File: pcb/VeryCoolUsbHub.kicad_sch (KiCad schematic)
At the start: 51 parts, among them U1 HD3SS3220RNHR, U2 HD3SS3220RNHR, X1 X322525MSB4SI, X2 X322525MSB4SI

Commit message: please tell me this is the last time i need to reroute
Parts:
- removed C10: CC0603KRX7R9BB104, EasyEDA:C0603, symbol EasyEDA:CC0603KRX7R9BB104
- removed USB_OUT1, USB_OUT2: HC-USB3.0-L168-WP, EasyEDA:USB-TH_USB3.0-A, symbol EasyEDA:HC-USB3.0-L168-WP
- added C33, C34, C35, C36, C37: CC0603KRX7R9BB104, EasyEDA:C0603, symbol EasyEDA:CC0603KRX7R9BB104
- added R4: R, Resistor_SMD:R_0402_1005Metric, symbol Device:R
- added USB_OUT_1, USB_OUT_2: HC-ST-003-01-J, EasyEDA:USB-3.0-A-TH_HC-ST-003-01-Z, symbol EasyEDA:HC-ST-003-01-J
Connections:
- net DN1: now also USB_OUT_1.2 (D-)
- net DN2: now also USB_OUT_2.2 (D-)
- net DP1: now also USB_OUT_1.3 (D+)
- net DP2: now also USB_OUT_2.3 (D+)
- net GND: now also USBC_OUT_1.0 (EH), C34.2, C35.2, R4.2, USB_OUT_1.10 (SHELL), USB_OUT_1.11 (SHELL), USB_OUT_1.4 (GND), USB_OUT_1.7 (GND_DRAIN), USB_OUT_2.10 (SHELL), USB_OUT_2.4 (GND), USB_OUT_2.7 (GND_DRAIN); no longer C11.2
- net VBUS: now also C34.1, USB_OUT_1.1 (Vbus); no longer C11.1
- net at ETHERNET_CONTROLLER1.38 (RSET): now also R4.1
- net RXn0 renamed RXN0
- net RXn1 renamed RXN1
- net RXN1: now also USB_OUT_1.5 (StdA_SSRX-)
- net RXn2 renamed RXN2
- net RXN2: now also USB_OUT_2.5 (StdA_SSRX-)
- net RXn3 renamed RXN3
- net RXn4 renamed RXN4
- net RXp0 renamed RXP0
- net RXp1 renamed RXP1
- net RXP1: now also USB_OUT_1.6 (StdA_SSRX+)
- net RXp2 renamed RXP2
- net RXP2: now also USB_OUT_2.6 (StdA_SSRX+)
- net RXp3 renamed RXP3
- net RXp4 renamed RXP4
- net Txn0 renamed TXN0
- net Txn1 renamed TXN1
- net TXN1: now also C11.2
- net Txn2 renamed TXN2
- net TXN2: now also C36.2
- net Txn3 renamed TXN3
- net Txn4 renamed TXN4
- net Txp0 renamed TXP0
- net Txp1 renamed TXP1
- net TXP1: now also C33.2
- net Txp2 renamed TXP2
- net TXP2: now also C37.2
- net Txp3 renamed TXP3
- net Txp4 renamed TXP4
- new net: C33.1, USB_OUT_1.9 (StdA_SSTX+)
- new net: C37.1, USB_OUT_2.9 (StdA_SSTX+)
- new net: C11.1, USB_OUT_1.8 (StdA_SSTX-)
- new net: C36.1, USB_OUT_2.8 (StdA_SSTX-)
- new net: C35.1, USB_OUT_2.1 (Vbus)

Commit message: LETSGO THIS GONNA BE THE LAST TIME I ROUTE
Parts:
- added C10, C26: CC0603KRX7R9BB104, EasyEDA:C0603, symbol EasyEDA:CC0603KRX7R9BB104
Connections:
- net RXN1: now also USB_OUT_1.6 (StdA_SSRX+); no longer USB_OUT_1.5 (StdA_SSRX-)
- net RXN2: now also USB_OUT_2.6 (StdA_SSRX+); no longer USB_OUT_2.5 (StdA_SSRX-)
- net RXN4: now also ETHERNET_CONTROLLER1.16 (U3SSRXP); no longer ETHERNET_CONTROLLER1.15 (U3SSRXN)
- net RXP1: now also USB_OUT_1.5 (StdA_SSRX-); no longer USB_OUT_1.6 (StdA_SSRX+)
- net RXP2: now also USB_OUT_2.5 (StdA_SSRX-); no longer USB_OUT_2.6 (StdA_SSRX+)
- net RXP4: now also ETHERNET_CONTROLLER1.15 (U3SSRXN); no longer ETHERNET_CONTROLLER1.16 (U3SSRXP)
- net TXN1: now also C33.2; no longer C11.2
- net TXN2: now also C37.2; no longer C36.2
- net TXN4: now also ETHERNET_CONTROLLER1.13 (U3SSTXP); no longer ETHERNET_CONTROLLER1.12 (U3SSTXN)
- net TXP1: now also C11.2; no longer C33.2
- net TXP2: now also C36.2; no longer C37.2
- net TXP4: now also ETHERNET_CONTROLLER1.12 (U3SSTXN); no longer ETHERNET_CONTROLLER1.13 (U3SSTXP)
- net USBC_IN_TXN1: now also C9.2; no longer C8.1
- net USBC_IN_TXN2: now also C20.1; no longer C21.1
- net USBC_IN_TXP1: now also C8.1; no longer C9.2
- net USBC_IN_TXP2: now also C21.1; no longer C20.1
- net USBC_OUT_TXN1: now also C10.2; no longer U1.16 (TX1n)
- net USBC_OUT_TXN2: now also C23.1; no longer C24.1
- net USBC_OUT_TXP1: now also C26.1; no longer U1.17 (TX1p)
- net USBC_OUT_TXP2: now also C24.1; no longer C23.1
- net VBUS: now also C35.1, USB_OUT_2.1 (Vbus)
- new net: C10.1, U1.17 (TX1p)
- new net: C26.2, U1.16 (TX1n)
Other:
- moved on the sheet: C9

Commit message: maybedone?
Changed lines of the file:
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@@
 		)
 		(property "Description" "10kΩ ±1%/62.5mW/0402"
-			(at 99.568 255.016 0)
+			(at 98.806 255.016 0)
 			(effects
 				(font
@@
 			)
 		)
-		(property "Datasheet" "https://www.lcsc.com/datasheet/C871499.pdf"
+		(property "Datasheet" "https://www.lcsc.com/datasheet/C871726.pdf"
 			(at 193.04 93.98 0)
 			(effects

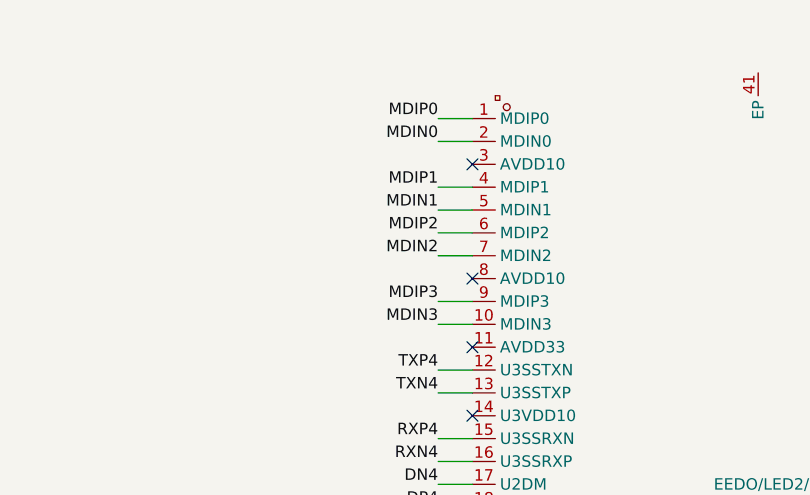
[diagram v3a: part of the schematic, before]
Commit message: reroute a litlle bit of ethernet port
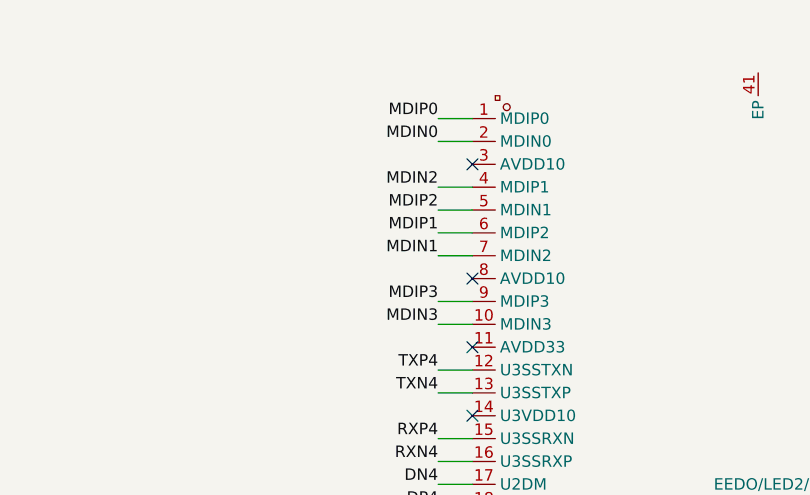
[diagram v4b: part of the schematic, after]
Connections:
- net MDIN1: now also ETHERNET_CONTROLLER1.7 (MDIN2); no longer ETHERNET_CONTROLLER1.5 (MDIN1)
- net MDIN2: now also ETHERNET_CONTROLLER1.4 (MDIP1); no longer ETHERNET_CONTROLLER1.7 (MDIN2)
- net MDIP1: now also ETHERNET_CONTROLLER1.6 (MDIP2); no longer ETHERNET_CONTROLLER1.4 (MDIP1)
- net MDIP2: now also ETHERNET_CONTROLLER1.5 (MDIN1); no longer ETHERNET_CONTROLLER1.6 (MDIP2)
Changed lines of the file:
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@@
-		)
-	)
-	(label "MDIN2"
-		(at 438.15 52.07 180)
-		(effects
-			(font
-				(size 1.27 1.27)
-			)
-			(justify right bottom)
 		)
 	)
@@
 		)
 	)
+	(label "MDIN1"
+		(at 438.15 52.07 180)
+		(effects
+			(font
+				(size 1.27 1.27)
+			)
+			(justify right bottom)
+		)
+	)
 	(label "TXP2"
 		(at 147.32 217.17 0)
@@
 		)
 	)
-	(label "MDIP1"
-		(at 438.15 44.45 180)
-		(effects
-			(font
-				(size 1.27 1.27)
-			)
-			(justify right bottom)
-		)
-	)
 	(label "RXN2"
 		(at 147.32 212.09 0)
@@
 		)
 	)
-	(label "MDIP2"
-		(at 438.15 49.53 180)
-		(effects
-			(font
-				(size 1.27 1.27)
-			)
-			(justify right bottom)
-		)
-	)
 	(label "RXP3"
 		(at 104.14 209.55 180)
@@
 		)
 	)
+	(label "MDIP1"
+		(at 438.15 49.53 180)
+		(effects
+			(font
+				(size 1.27 1.27)
+			)
+			(justify right bottom)
+		)
+	)
 	(label "USBC_OUT_RXP1"
 		(at 83.82 92.71 180)
@@
 		)
 	)
+	(label "MDIP2"
+		(at 438.15 46.99 180)
+		(effects
+			(font
+				(size 1.27 1.27)
+			)
+			(justify right bottom)
+		)
+	)
 	(label "RXN0"
 		(at 146.05 257.81 0)
@@
 		)
 	)
+	(label "MDIN2"
+		(at 438.15 44.45 180)
+		(effects
+			(font
+				(size 1.27 1.27)
+			)
+			(justify right bottom)
+		)
+	)
 	(label "USBC_IN_TXN2"
 		(at 295.91 347.98 180)
@@
 		(effects
 			(font
-				(size 1.27 1.27)
-			)
-			(justify right bottom)
-		)
-	)
-	(label "MDIN1"
-		(at 438.15 46.99 180)
-		(effects
-			(font

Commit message: change schen
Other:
- note added: "ETHERNET"
- note added: "USB A OUT"
- note added: "USB C IN"
- note added: "USB C OUT"
- note added: "USB CONTROLLER"
- moved on the sheet: C17, C18, C25, C5, R2, R3, USB_CONTROLLER1, X2

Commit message: forgor to update
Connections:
- net USB_TXN1: now reaches C33.1, USB_OUT_1.9 (StdA_SSTX+)
- net TXN2+: now reaches C37.1, USB_OUT_2.9 (StdA_SSTX+)
- net IN_C_TXN2: now reaches C20.2, U2.21 (TX2p)
- net USB_TXP1: now reaches C11.1, USB_OUT_1.8 (StdA_SSTX-)
- net IN_C_TXP2: now reaches C21.2, U2.20 (TX2n)
- net C_TXN1: now reaches C10.1, U1.17 (TX1p)
- net C_TXN2: now reaches C23.2, U1.21 (TX2p)
- net TXN2-: now reaches C36.1, USB_OUT_2.8 (StdA_SSTX-)
- net IN_C_TXP1: now reaches C8.2, U2.16 (TX1n)
- net C_TXP2: now reaches C24.2, U1.20 (TX2n)
- net C_TXP1: now reaches C26.2, U1.16 (TX1n)
- net IN_C_TXN1: now reaches C9.1, U2.17 (TX1p)
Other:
- moved on the sheet: C10, C20, C23, C24

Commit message: fixed some signal intergrity problem
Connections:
- net GND: now also U1.31 (EP), U2.31 (EP)
- no-connect marks 60 -> 58
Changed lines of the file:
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@@
 	)
 	(no_connect
-		(at 270.51 55.88)
-	)
-	(no_connect
 		(at 288.29 219.71)
 	)
 	(no_connect
-		(at 464.82 284.48)
-	)
-	(no_connect
 		(at 474.98 284.48)
 	)
@@
 	)
 	(symbol
+		(lib_id "power:GND")
+		(at 270.51 55.88 180)
+		(unit 1)
+		(exclude_from_sim no)
+		(in_bom yes)
+		(on_board yes)
+		(dnp no)
+		(fields_autoplaced yes)
+		(property "Reference" "#PWR029"
+			(at 270.51 49.53 0)
+			(effects
+				(font
+					(size 1.27 1.27)
+				)
+				(hide yes)
+			)
+		)
+		(property "Value" "GND"
+			(at 270.51 50.8 0)
+			(effects
+				(font
+					(size 1.27 1.27)
+				)
+			)
+		)
+		(property "Footprint" ""
+			(at 270.51 55.88 0)
+			(effects
+				(font
+					(size 1.27 1.27)
+				)
+				(hide yes)
+			)
+		)
+		(property "Datasheet" ""
+			(at 270.51 55.88 0)
+			(effects
+				(font
+					(size 1.27 1.27)
+				)
+				(hide yes)
+			)
+		)
+		(property "Description" "Power symbol creates a global label with name \"GND\" , ground"
+			(at 270.51 55.88 0)
+			(effects
+				(font
+					(size 1.27 1.27)
+				)
+				(hide yes)
+			)
+		)
+		(pin "1"
+		)
+		(instances
+			(project "VeryCoolUsbHub"
+				(path "/a66e963d-9223-4dd6-b11b-c5e7c640f212"
+					(reference "#PWR029")
+					(unit 1)
+				)
+			)
+		)
+	)
+	(symbol
 		(lib_id "EasyEDA:RC0603FR-07200KL")
 		(at 454.66 350.52 0)
@@
 					(unit 1)
 				)
+			)
+		)
+	)
+	(symbol
+		(lib_id "power:GND")
+		(at 464.82 284.48 180)
+		(unit 1)
+		(exclude_from_sim no)
+		(in_bom yes)
+		(on_board yes)
+		(dnp no)
+		(fields_autoplaced yes)
+		(property "Reference" "#PWR034"
+			(at 464.82 278.13 0)
+			(effects
+				(font
+					(size 1.27 1.27)
+				)
+				(hide yes)
+			)
+		)
+		(property "Value" "GND"
+			(at 464.82 279.4 0)
+			(effects
+				(font
+					(size 1.27 1.27)
+				)
+			)
+		)
+		(property "Footprint" ""
+			(at 464.82 284.48 0)
+			(effects
+				(font
+					(size 1.27 1.27)
+				)
+				(hide yes)
+			)
+		)
+		(property "Datasheet" ""
+			(at 464.82 284.48 0)
+			(effects
+				(font
+					(size 1.27 1.27)
+				)
+				(hide yes)
+			)
+		)
+		(property "Description" "Power symbol creates a global label with name \"GND\" , ground"
+			(at 464.82 284.48 0)
+			(effects
+				(font
+					(size 1.27 1.27)
+				)
+				(hide yes)
+			)
+		)
+		(pin "1"
+		)
+		(instances
+			(project "VeryCoolUsbHub"
+				(path "/a66e963d-9223-4dd6-b11b-c5e7c640f212"
+					(reference "#PWR034")
+					(unit 1)
+				)

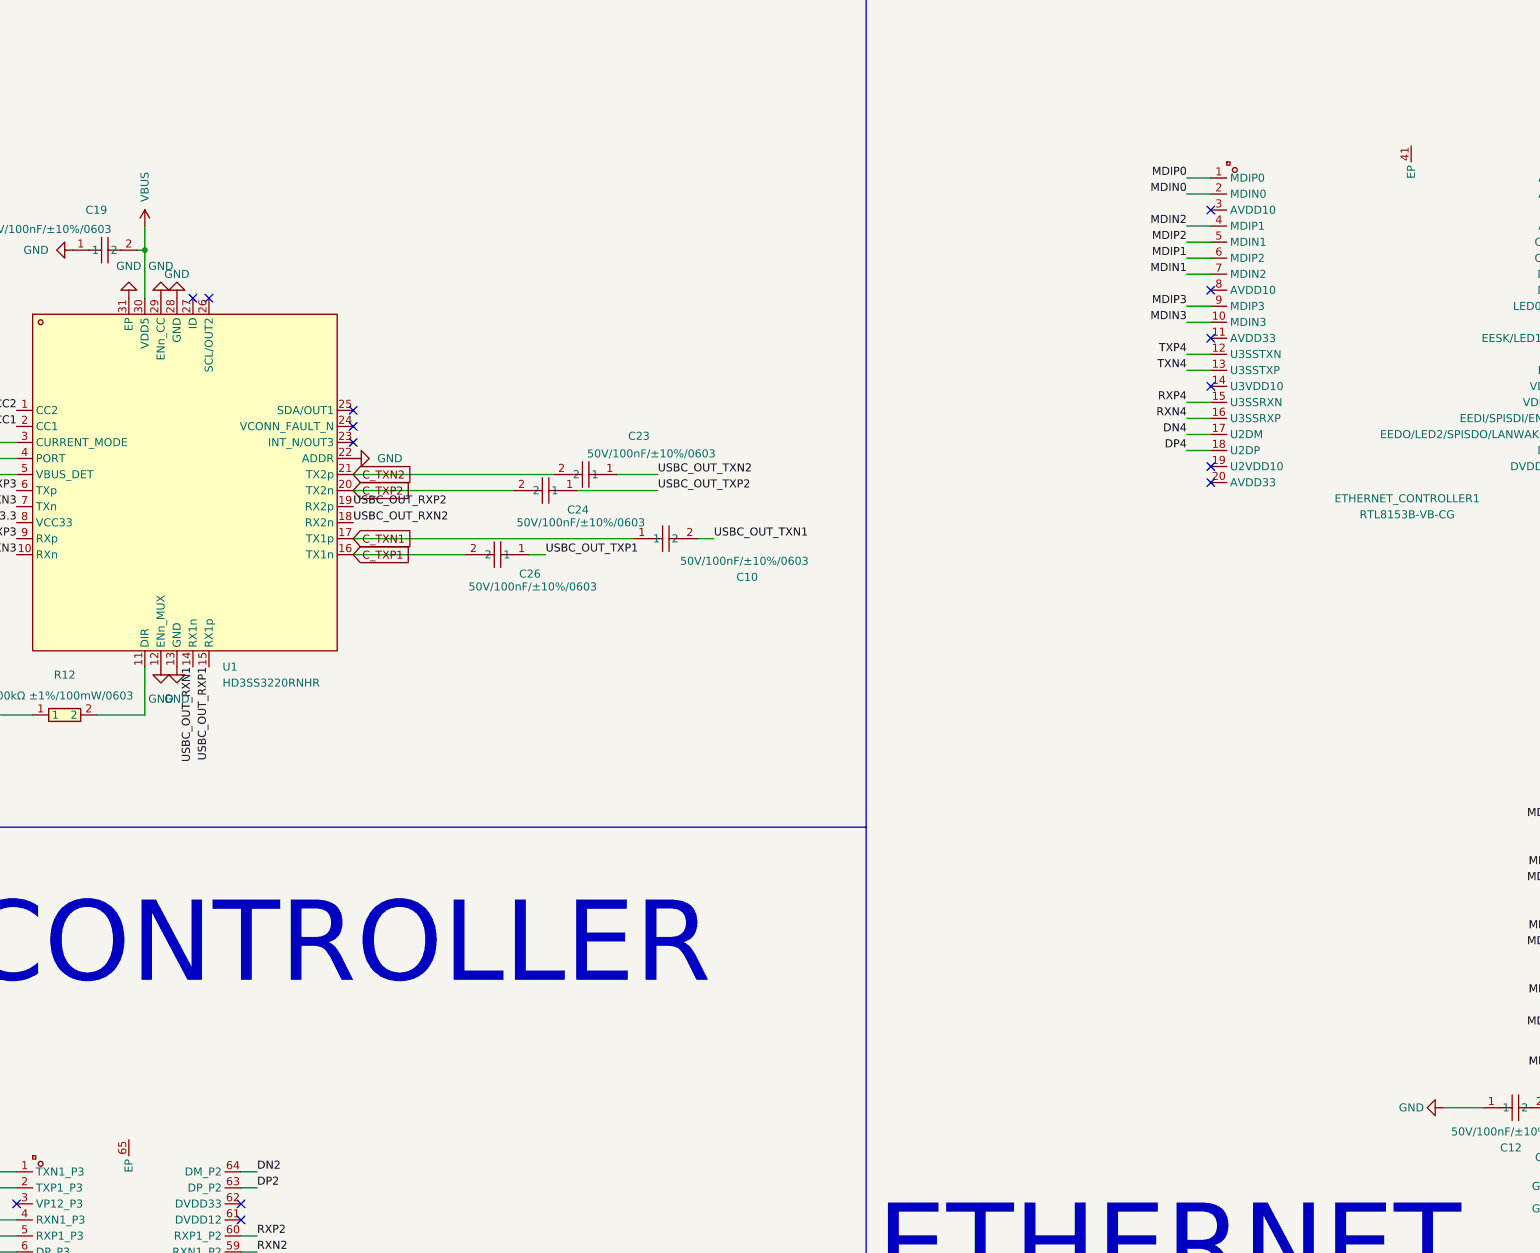
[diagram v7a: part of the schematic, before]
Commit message: fixed small error in pcb
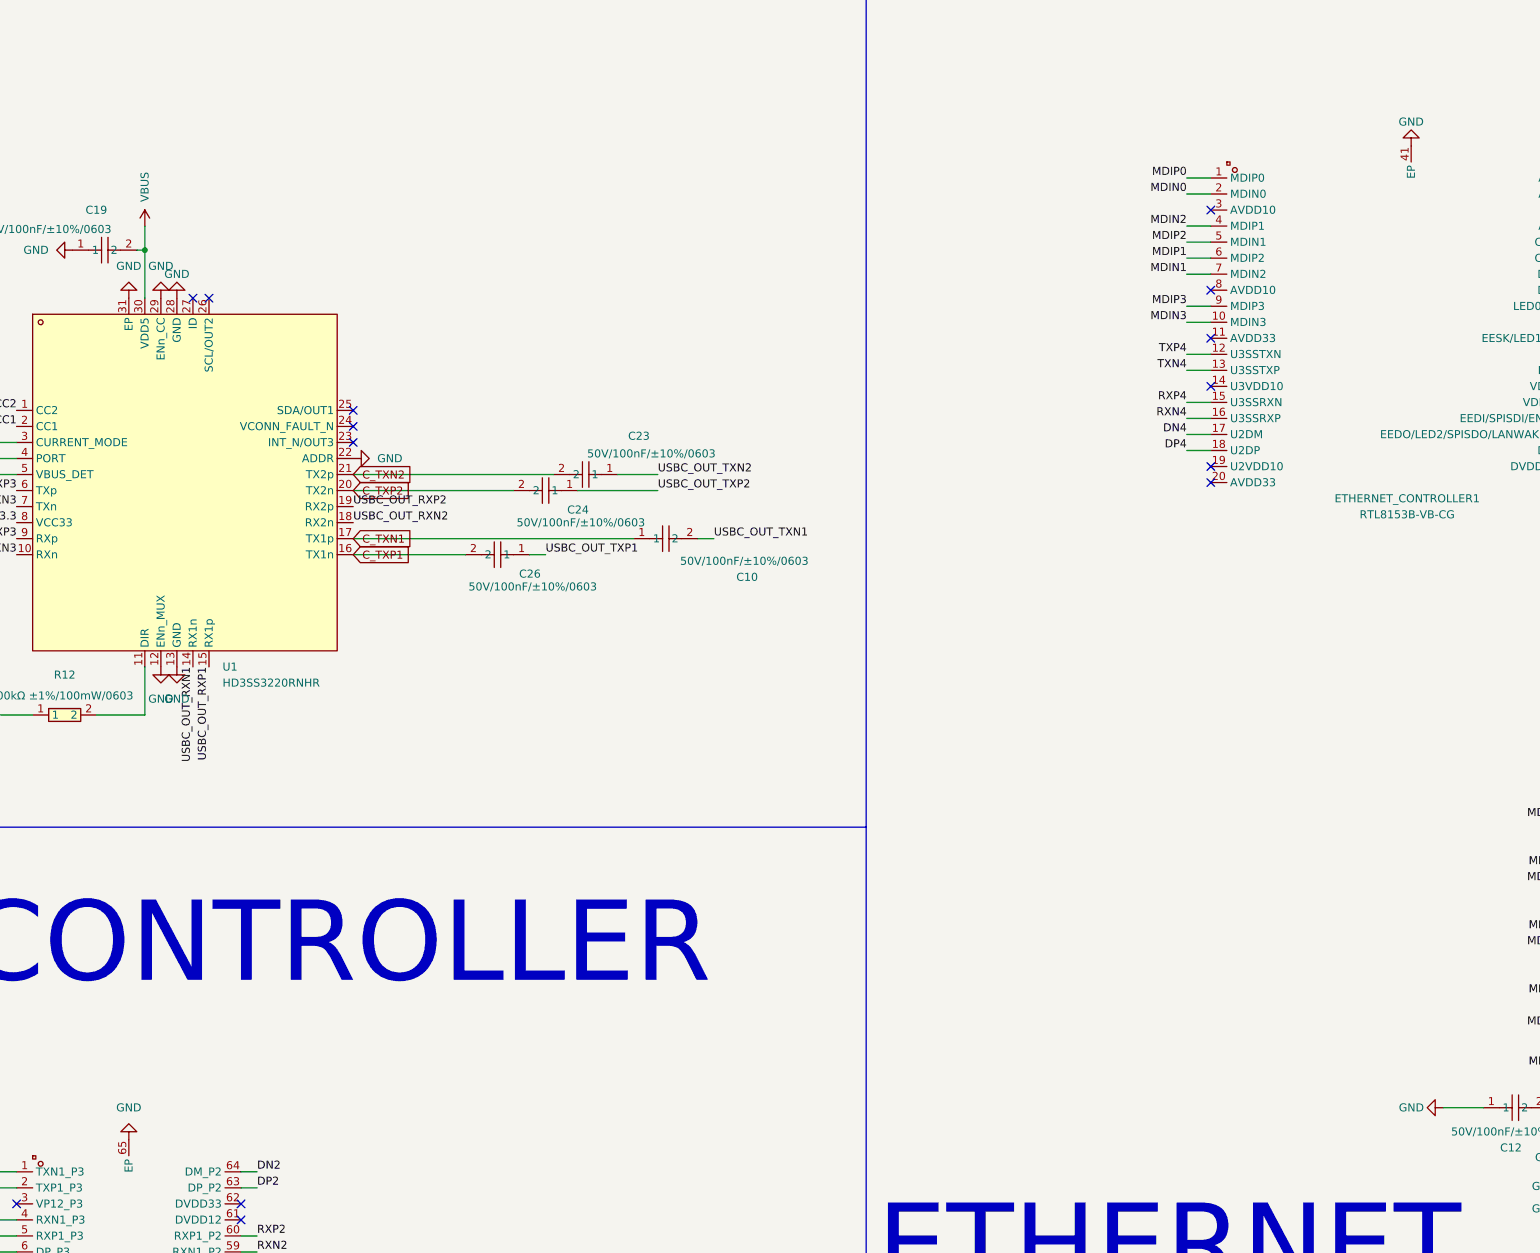
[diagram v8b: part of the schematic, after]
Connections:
- net GND: now also ETHERNET_CONTROLLER1.41 (EP), USB_CONTROLLER1.65 (EP)
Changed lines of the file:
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@@
+	(symbol
+		(lib_id "power:GND")
+		(at 473.71 31.75 180)
+		(unit 1)
+		(exclude_from_sim no)
+		(in_bom yes)
+		(on_board yes)
+		(dnp no)
+		(property "Reference" "#PWR055"
+			(at 473.71 25.4 0)
+			(effects
+				(font
+					(size 1.27 1.27)
+				)
+				(hide yes)
+			)
+		)
+		(property "Value" "GND"
+			(at 473.71 27.94 0)
+			(effects
+				(font
+					(size 1.27 1.27)
+				)
+			)
+		)
+		(property "Footprint" ""
+			(at 473.71 31.75 0)
+			(effects
+				(font
+					(size 1.27 1.27)
+				)
+				(hide yes)
+			)
+		)
+		(property "Datasheet" ""
+			(at 473.71 31.75 0)
+			(effects
+				(font
+					(size 1.27 1.27)
+				)
+				(hide yes)
+			)
+		)
+		(property "Description" "Power symbol creates a global label with name \"GND\" , ground"
+			(at 473.71 31.75 0)
+			(effects
+				(font
+					(size 1.27 1.27)
+				)
+				(hide yes)
+			)
+		)
+		(pin "1"
+		)
+		(instances
+			(project "VeryCoolUsbHub"
+				(path "/a66e963d-9223-4dd6-b11b-c5e7c640f212"
+					(reference "#PWR055")
+					(unit 1)
+				)
+			)
+		)
+	)
 	(symbol
 		(lib_id "power:GND")
@@
 					(unit 1)
 				)
+			)
+		)
+	)
+	(symbol
+		(lib_id "power:GND")
+		(at 270.51 189.23 180)
+		(unit 1)
+		(exclude_from_sim no)
+		(in_bom yes)
+		(on_board yes)
+		(dnp no)
+		(fields_autoplaced yes)
+		(property "Reference" "#PWR035"
+			(at 270.51 182.88 0)
+			(effects
+				(font
+					(size 1.27 1.27)
+				)
+				(hide yes)
+			)
+		)
+		(property "Value" "GND"
+			(at 270.51 184.15 0)
+			(effects
+				(font
+					(size 1.27 1.27)
+				)
+			)
+		)
+		(property "Footprint" ""
+			(at 270.51 189.23 0)
+			(effects
+				(font
+					(size 1.27 1.27)
+				)
+				(hide yes)
+			)
+		)
+		(property "Datasheet" ""
+			(at 270.51 189.23 0)
+			(effects
+				(font
+					(size 1.27 1.27)
+				)
+				(hide yes)
+			)
+		)
+		(property "Description" "Power symbol creates a global label with name \"GND\" , ground"
+			(at 270.51 189.23 0)
+			(effects
+				(font
+					(size 1.27 1.27)
+				)
+				(hide yes)
+			)
+		)
+		(pin "1"
+		)
+		(instances
+			(project ""
+				(path "/a66e963d-9223-4dd6-b11b-c5e7c640f212"
+					(reference "#PWR035")
+					(unit 1)
+				)
